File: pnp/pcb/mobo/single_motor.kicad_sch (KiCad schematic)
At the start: 9 parts, among them J21 TMC_PIN_HEADER, M3 Stepper_Motor

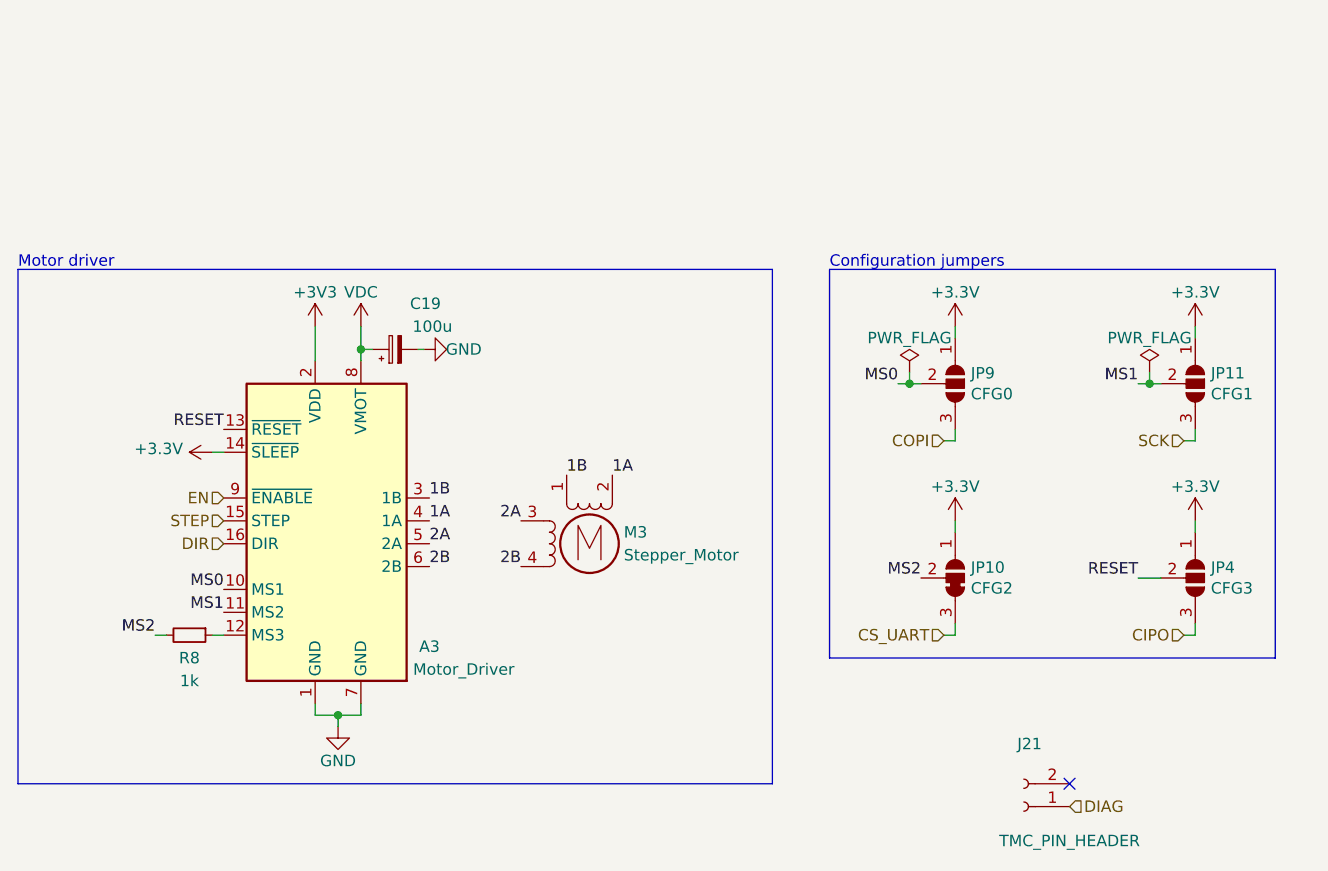
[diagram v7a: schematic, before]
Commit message: adds and routes boot jumper header for external boot button
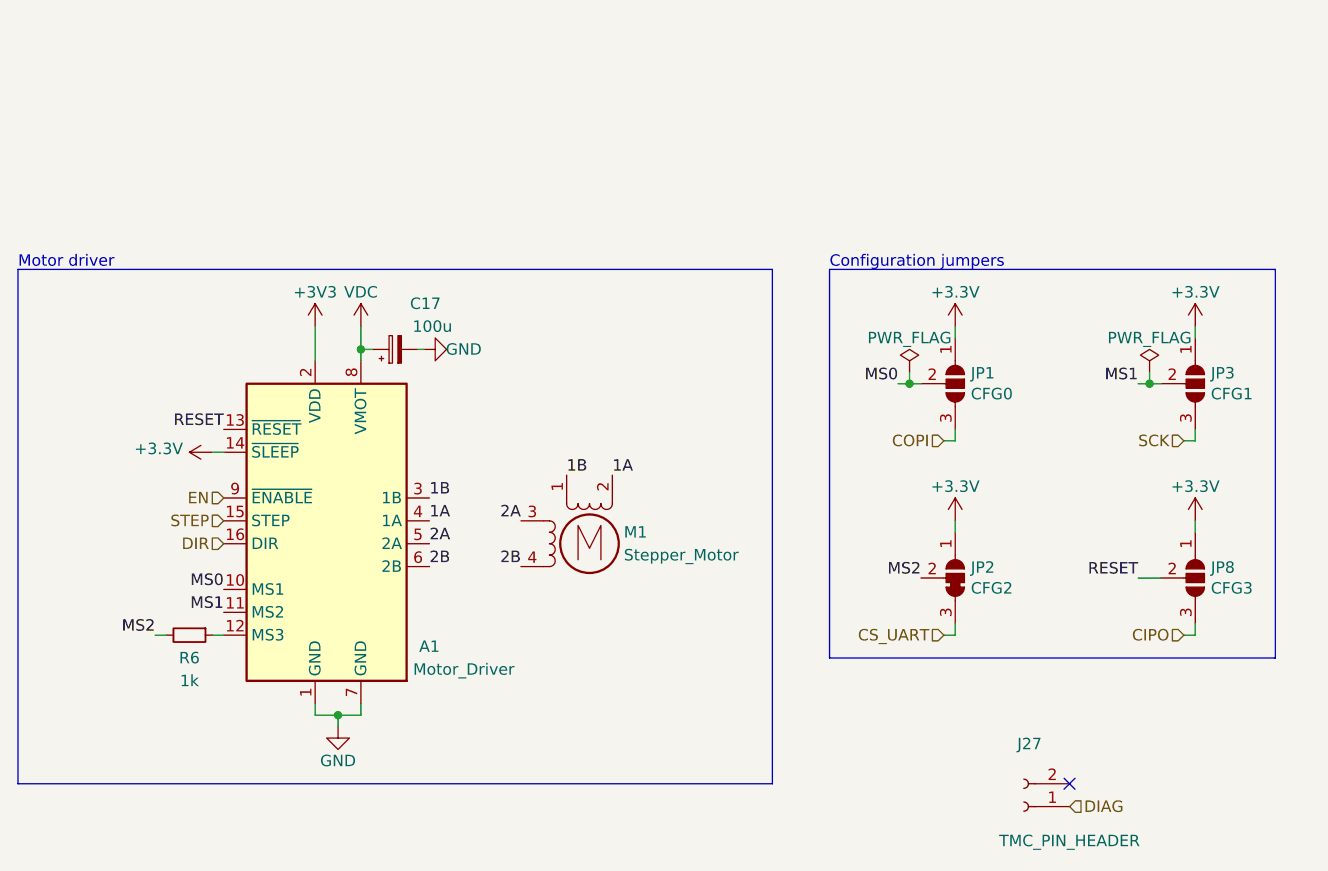
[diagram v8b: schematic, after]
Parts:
- renumbered A3 to A1, C19 to C17, J21 to J27, JP9 to JP1, JP10 to JP2, JP11 to JP3, JP4 to JP8, M3 to M1, R8 to R6
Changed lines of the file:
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@@
   (symbol (lib_id "power:+3.3V") (at 208.28 105.41 0)
     (in_bom yes) (on_board yes)
-    (property "Reference" "#PWR0204" (id 0) (at 208.28 109.22 0)
+    (property "Reference" "#PWR0213" (id 0) (at 208.28 109.22 0)
       (effects (font (size 1.27 1.27)) hide)
     )
@@
   (symbol (lib_id "Device:R_Small") (at 96.52 118.11 270)
     (in_bom yes) (on_board yes)
-    (property "Reference" "R8" (id 0) (at 96.52 120.65 90))
+    (property "Reference" "R6" (id 0) (at 96.52 120.65 90))
     (property "Value" "1k" (id 1) (at 96.52 123.19 90))
     (property "Footprint" "Resistor_SMD:R_0805_2012Metric" (id 2) (at 96.52 116.332 90)
@@
   (symbol (lib_id "power:+3.3V") (at 181.61 83.82 0)
     (in_bom yes) (on_board yes)
-    (property "Reference" "#PWR0205" (id 0) (at 181.61 87.63 0)
+    (property "Reference" "#PWR0214" (id 0) (at 181.61 87.63 0)
       (effects (font (size 1.27 1.27)) hide)
     )
@@
   (symbol (lib_id "power:GND") (at 113.03 128.27 0)
     (in_bom yes) (on_board yes)
-    (property "Reference" "#PWR0211" (id 0) (at 113.03 134.62 0)
+    (property "Reference" "#PWR0220" (id 0) (at 113.03 134.62 0)
       (effects (font (size 1.27 1.27)) hide)
     )
@@
   (symbol (lib_id "power:+3.3V") (at 99.06 97.79 90)
     (in_bom yes) (on_board yes)
-    (property "Reference" "#PWR0208" (id 0) (at 102.87 97.79 0)
+    (property "Reference" "#PWR0217" (id 0) (at 102.87 97.79 0)
       (effects (font (size 1.27 1.27)) hide)
     )
@@
   (symbol (lib_id "power:PWR_FLAG") (at 203.2 88.9 0)
     (in_bom yes) (on_board yes)
-    (property "Reference" "#FLG0110" (id 0) (at 203.2 86.995 0)
+    (property "Reference" "#FLG0113" (id 0) (at 203.2 86.995 0)
       (effects (font (size 1.27 1.27)) hide)
     )
@@
   (symbol (lib_id "power:+3.3V") (at 181.61 105.41 0)
     (in_bom yes) (on_board yes)
-    (property "Reference" "#PWR0203" (id 0) (at 181.61 109.22 0)
+    (property "Reference" "#PWR0212" (id 0) (at 181.61 109.22 0)
       (effects (font (size 1.27 1.27)) hide)
     )
@@
   (symbol (lib_id "Driver_Motor:Pololu_Breakout_A4988") (at 110.49 105.41 0)
     (in_bom yes) (on_board yes)
-    (property "Reference" "A3" (id 0) (at 123.19 119.38 0))
+    (property "Reference" "A1" (id 0) (at 123.19 119.38 0))
     (property "Value" "Motor_Driver" (id 1) (at 127 121.92 0))
     (property "Footprint" "Module:Pololu_Breakout-16_15.2x20.3mm" (id 2) (at 117.475 124.46 0)
@@
   (symbol (lib_id "power:GND") (at 122.555 86.36 90)
     (in_bom yes) (on_board yes)
-    (property "Reference" "#PWR0207" (id 0) (at 128.905 86.36 0)
+    (property "Reference" "#PWR0216" (id 0) (at 128.905 86.36 0)
       (effects (font (size 1.27 1.27)) hide)
     )
@@
   (symbol (lib_id "power:+3.3V") (at 208.28 83.82 0)
     (in_bom yes) (on_board yes)
-    (property "Reference" "#PWR0206" (id 0) (at 208.28 87.63 0)
+    (property "Reference" "#PWR0215" (id 0) (at 208.28 87.63 0)
       (effects (font (size 1.27 1.27)) hide)
     )
@@
   (symbol (lib_id "power:VDC") (at 115.57 83.82 0)
     (in_bom yes) (on_board yes)
-    (property "Reference" "#PWR0210" (id 0) (at 115.57 86.36 0)
+    (property "Reference" "#PWR0219" (id 0) (at 115.57 86.36 0)
       (effects (font (size 1.27 1.27)) hide)
     )
@@
   (symbol (lib_id "Device:C_Polarized_Small") (at 119.38 86.36 90)
     (in_bom yes) (on_board yes)
-    (property "Reference" "C19" (id 0) (at 124.46 81.28 90)
+    (property "Reference" "C17" (id 0) (at 124.46 81.28 90)
       (effects (font (size 1.27 1.27)) (justify left))
     )
@@
   (symbol (lib_id "Jumper:SolderJumper_3_Open") (at 181.61 90.17 270)
     (in_bom yes) (on_board yes)
-    (property "Reference" "JP9" (id 0) (at 183.3372 89.0016 90)
+    (property "Reference" "JP1" (id 0) (at 183.3372 89.0016 90)
       (effects (font (size 1.27 1.27)) (justify left))
     )
@@
   (symbol (lib_id "power:PWR_FLAG") (at 176.53 88.9 0)
     (in_bom yes) (on_board yes)
-    (property "Reference" "#FLG0112" (id 0) (at 176.53 86.995 0)
+    (property "Reference" "#FLG0115" (id 0) (at 176.53 86.995 0)
       (effects (font (size 1.27 1.27)) hide)
     )
@@
   (symbol (lib_id "Jumper:SolderJumper_3_Open") (at 208.28 111.76 270)
     (in_bom yes) (on_board yes)
-    (property "Reference" "JP4" (id 0) (at 210.0072 110.5916 90)
+    (property "Reference" "JP8" (id 0) (at 210.0072 110.5916 90)
       (effects (font (size 1.27 1.27)) (justify left))
     )
@@
   (symbol (lib_id "power:+3V3") (at 110.49 83.82 0)
     (in_bom yes) (on_board yes)
-    (property "Reference" "#PWR0209" (id 0) (at 110.49 87.63 0)
+    (property "Reference" "#PWR0218" (id 0) (at 110.49 87.63 0)
       (effects (font (size 1.27 1.27)) hide)
     )
@@
   (symbol (lib_id "index:SolderJumper_3_Bridged23") (at 181.61 111.76 270) (mirror x)
     (in_bom yes) (on_board yes)
-    (property "Reference" "JP10" (id 0) (at 183.3372 110.5916 90)
+    (property "Reference" "JP2" (id 0) (at 183.3372 110.5916 90)
       (effects (font (size 1.27 1.27)) (justify left))
     )
@@
   (symbol (lib_id "Motor:Stepper_Motor_bipolar") (at 140.97 107.95 0)
     (in_bom yes) (on_board yes)
-    (property "Reference" "M3" (id 0) (at 144.78 106.68 0)
+    (property "Reference" "M1" (id 0) (at 144.78 106.68 0)
       (effects (font (size 1.27 1.27)) (justify left))
     )
@@
   (symbol (lib_id "Jumper:SolderJumper_3_Open") (at 208.28 90.17 270)
     (in_bom yes) (on_board yes)
-    (property "Reference" "JP11" (id 0) (at 210.0072 89.0016 90)
+    (property "Reference" "JP3" (id 0) (at 210.0072 89.0016 90)
       (effects (font (size 1.27 1.27)) (justify left))
     )
@@
   (symbol (lib_id "Connector:Conn_01x02_Female") (at 189.23 137.16 180)
     (in_bom yes) (on_board yes)
-    (property "Reference" "J21" (id 0) (at 189.865 130.1963 0))
+    (property "Reference" "J27" (id 0) (at 189.865 130.1963 0))
     (property "Value" "TMC_PIN_HEADER" (id 1) (at 194.31 140.97 0))
     (property "Footprint" "Connector_PinSocket_2.54mm:PinSocket_1x02_P2.54mm_Vertical" (id 2) (at 189.23 137.16 0)
